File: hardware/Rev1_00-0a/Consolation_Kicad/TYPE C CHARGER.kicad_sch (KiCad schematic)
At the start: 28 parts, among them J4 12401598E4#2A, J5 S2B-PH-K-S, U1 BQ25640VDLR

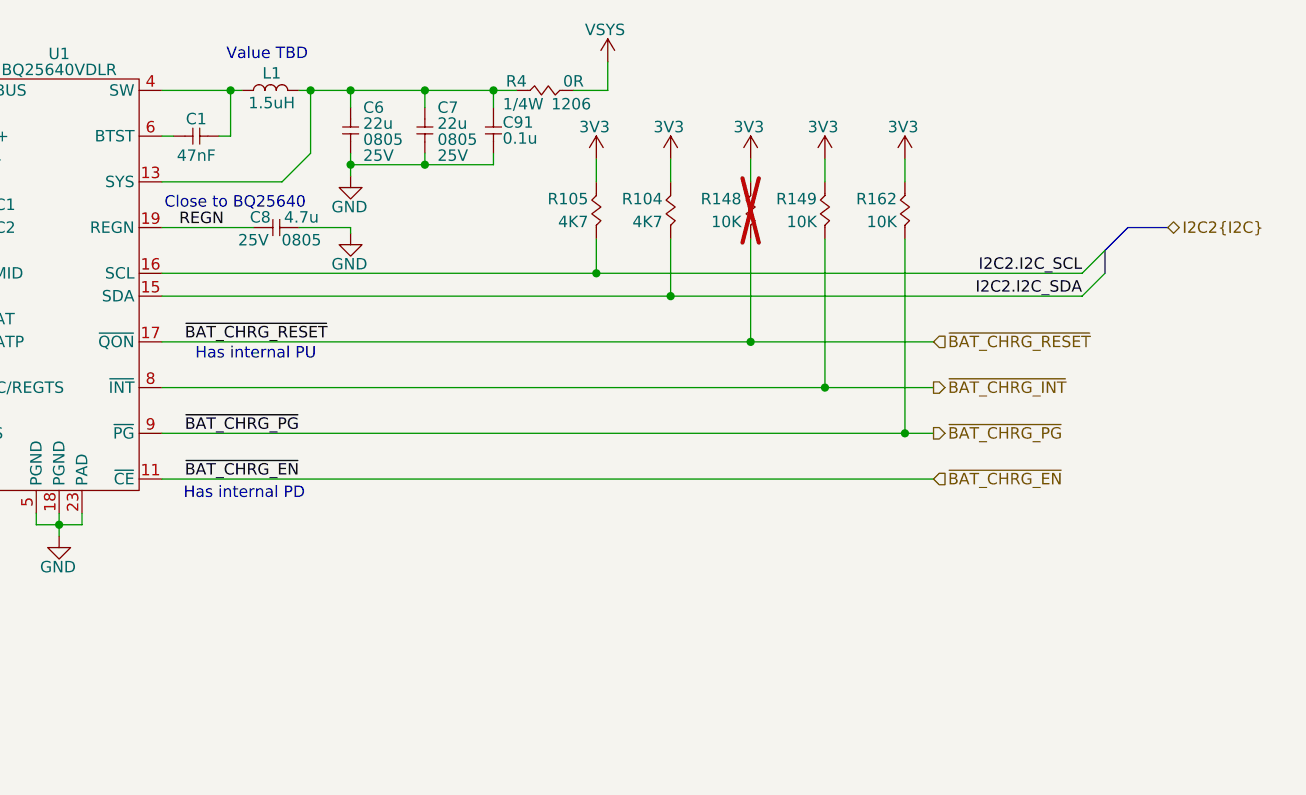
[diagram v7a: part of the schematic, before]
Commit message: Major update to consolation schematics to include - Power supply - RESET SUPERVISOR - Review of GPIO and pinmux
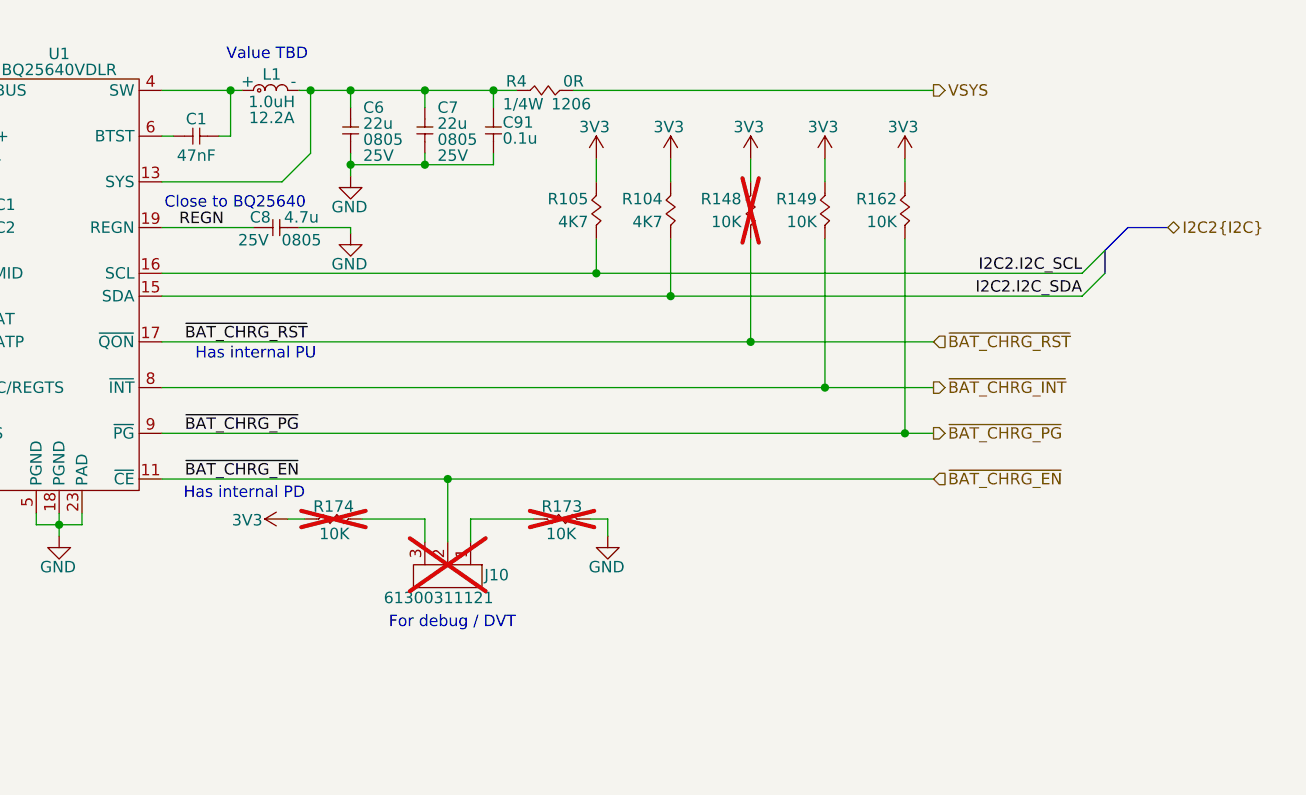
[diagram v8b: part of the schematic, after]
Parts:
- removed L1: PA5003.152NLT, footprint:PA5003, symbol KicadCompDb:Inductor/IND_00009
- added J10: 61300311121, footprint:HEADER_3P_2_54MM, symbol KicadCompDb:Connector/CONN_00001
- added L1: PA5003.102NLT, footprint:PA5003, symbol KicadCompDb:Inductor/IND_00012
- added R173, R174: 10K, footprint:RES_0402, symbol KicadCompDb:Resistors/RES_SMT_00013
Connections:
- net 3V3: now also R174.1
- net GND: now also R173.1
- net ~{BAT_CHRG_EN}: now also J10.2
- net at C6.2, C7.2, C91.2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: now also L1.2 (-)
- net at C1.1, U1.4 (SW): now also L1.1 (+)
- net ~{BAT_CHRG_RESET} renamed ~{BAT_CHRG_RST}
- new net: J10.1, R173.2
- new net: J10.3, R174.2
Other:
- note added: "For debug / DVT"
